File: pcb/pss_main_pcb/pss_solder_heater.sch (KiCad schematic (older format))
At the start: 43 parts, among them J3 Hot Air Gun, J4 Soldering Iron, Q1 BC817, Q2 MMBT2222, Q3 MMBT2907, Q4 IRLML9301T, Q5 IRFZ44S, Q6 BT139B-800, U3 MOC3023S, U4 LM358

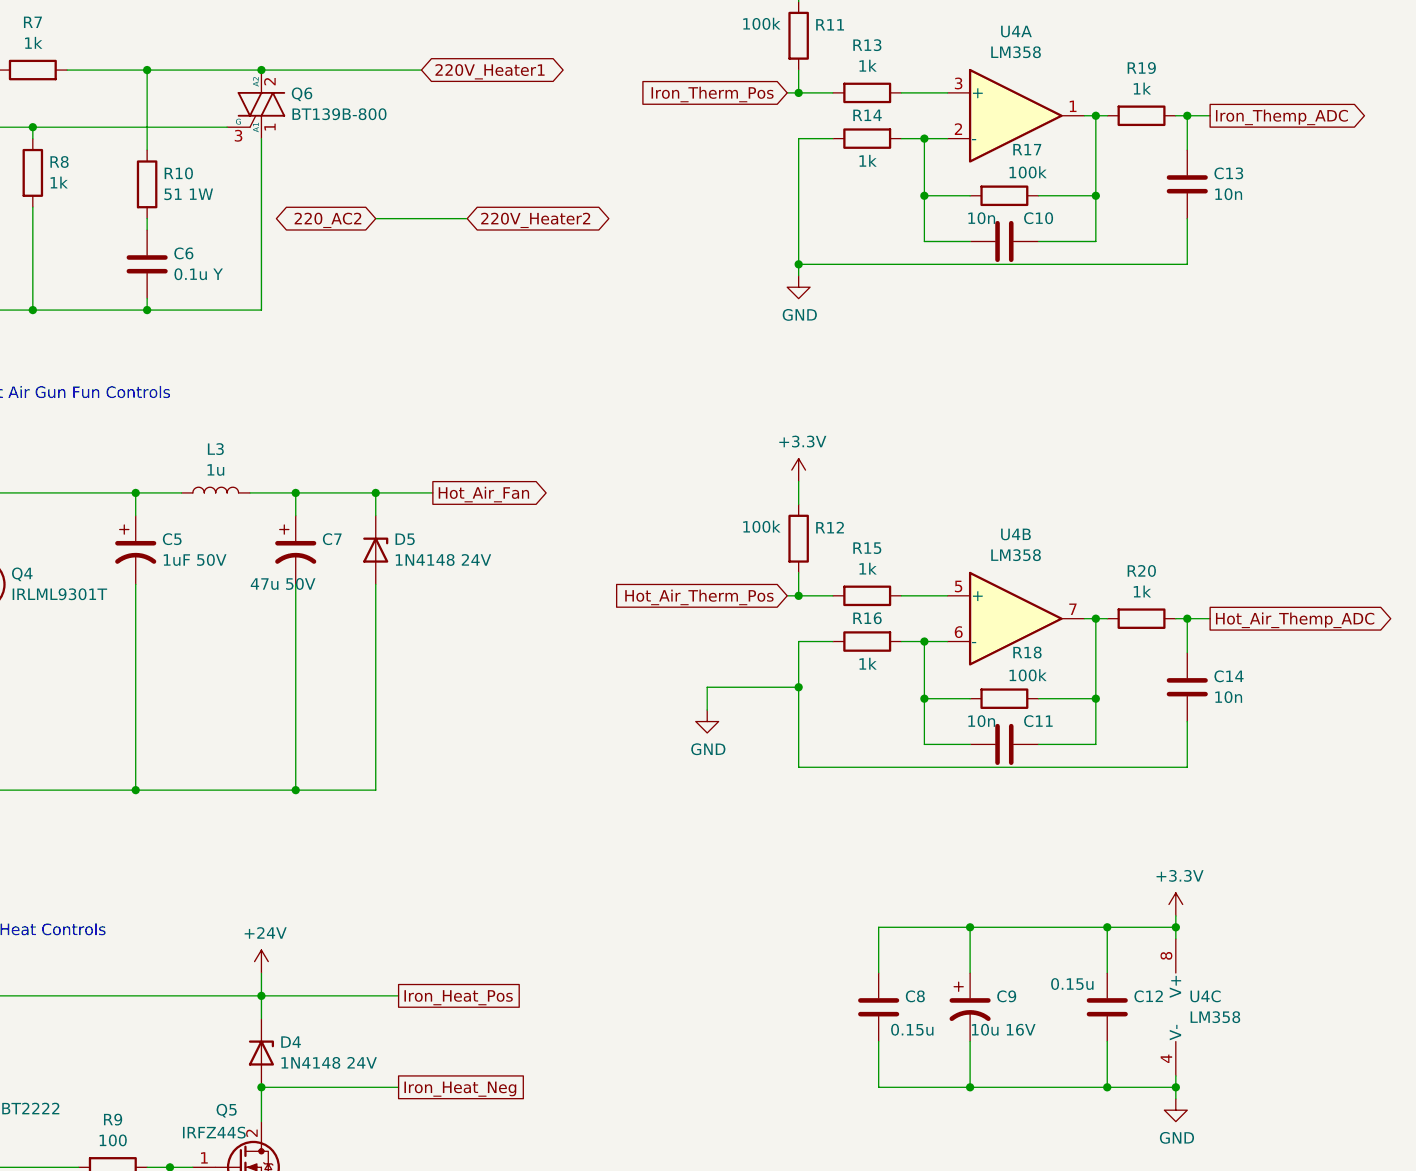
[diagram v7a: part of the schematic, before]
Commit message: Change footprints
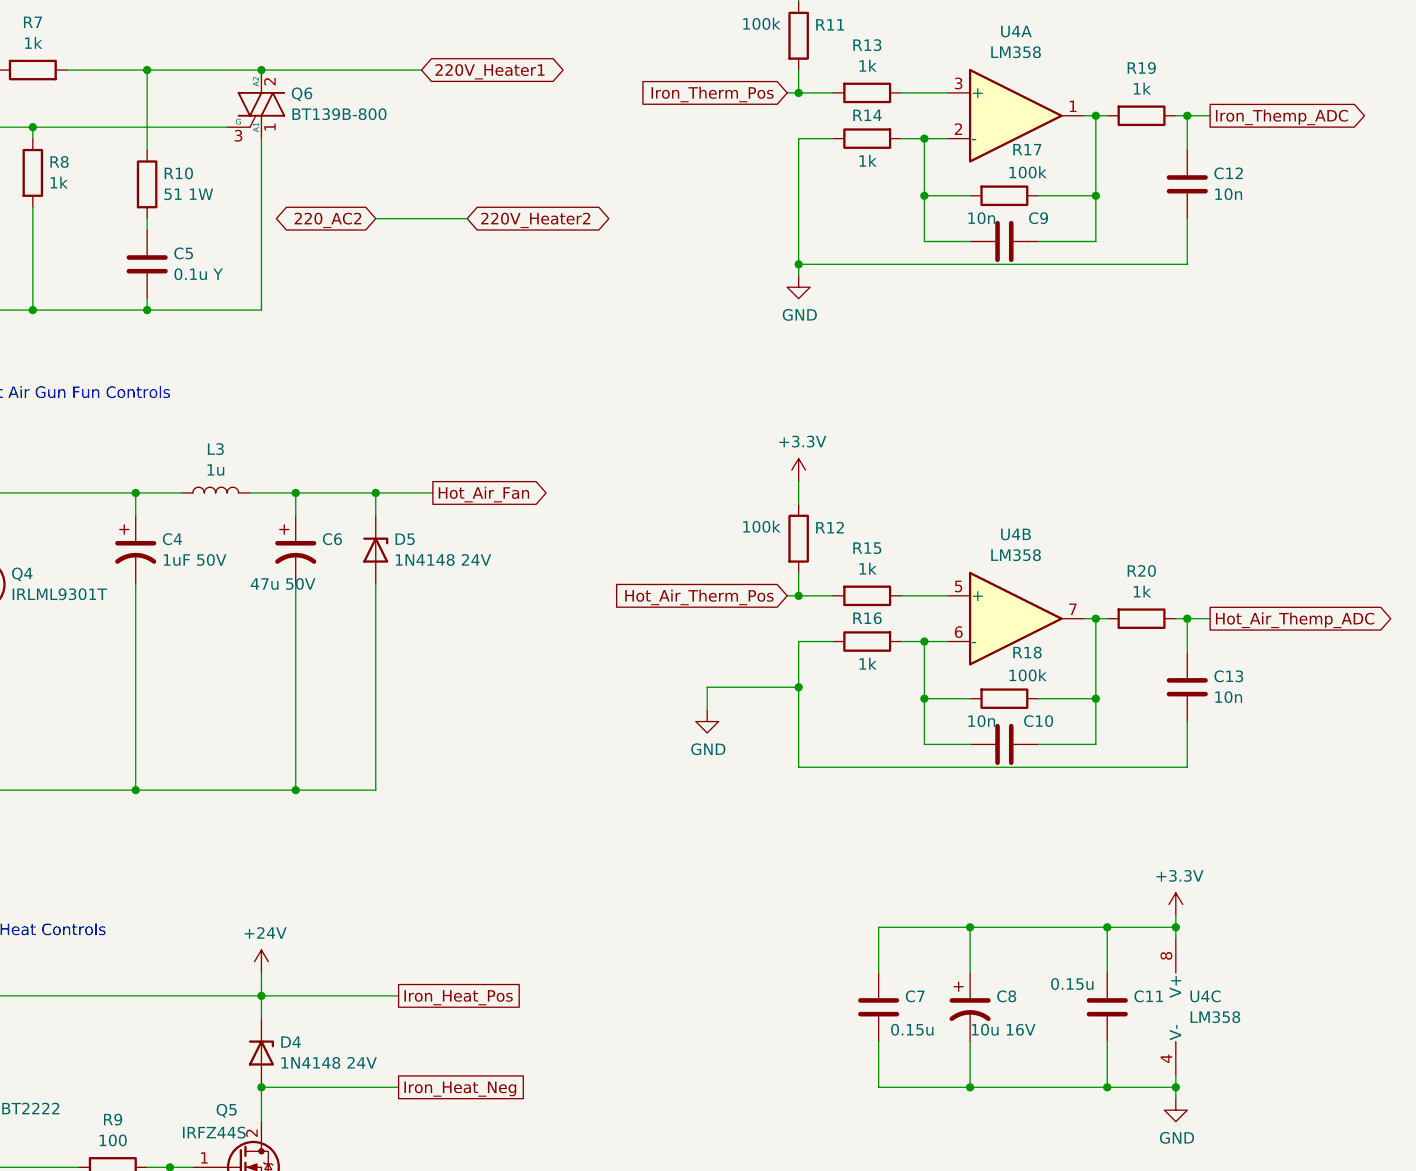
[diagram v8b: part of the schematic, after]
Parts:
- C4: renamed from C5; footprint Capacitor_SMD:CP_Elec_16x17.5 -> Capacitor_SMD:CP_Elec_4x5.4
- C6: renamed from C7; footprint Capacitor_SMD:CP_Elec_16x17.5 -> Capacitor_SMD:CP_Elec_8x10.5
- C8: renamed from C9; footprint Capacitor_SMD:CP_Elec_8x10.5 -> Capacitor_SMD:CP_Elec_4x5.4
- L3: footprint Inductor_SMD:L_Wuerth_HCI-1030 -> Inductor_SMD:L_Taiyo-Yuden_NR-30xx_HandSoldering
- Q5: footprint Package_TO_SOT_THT:TO-220-3_Vertical -> Package_TO_SOT_SMD:TO-263-2
- renumbered C11 to C10, C12 to C11, C13 to C12, C14 to C13, C6 to C5, C8 to C7, C10 to C9
